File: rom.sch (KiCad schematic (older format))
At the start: 13 parts, among them U3 23128_BASIC, U4 23128_KERNAL, U90 74HCT08

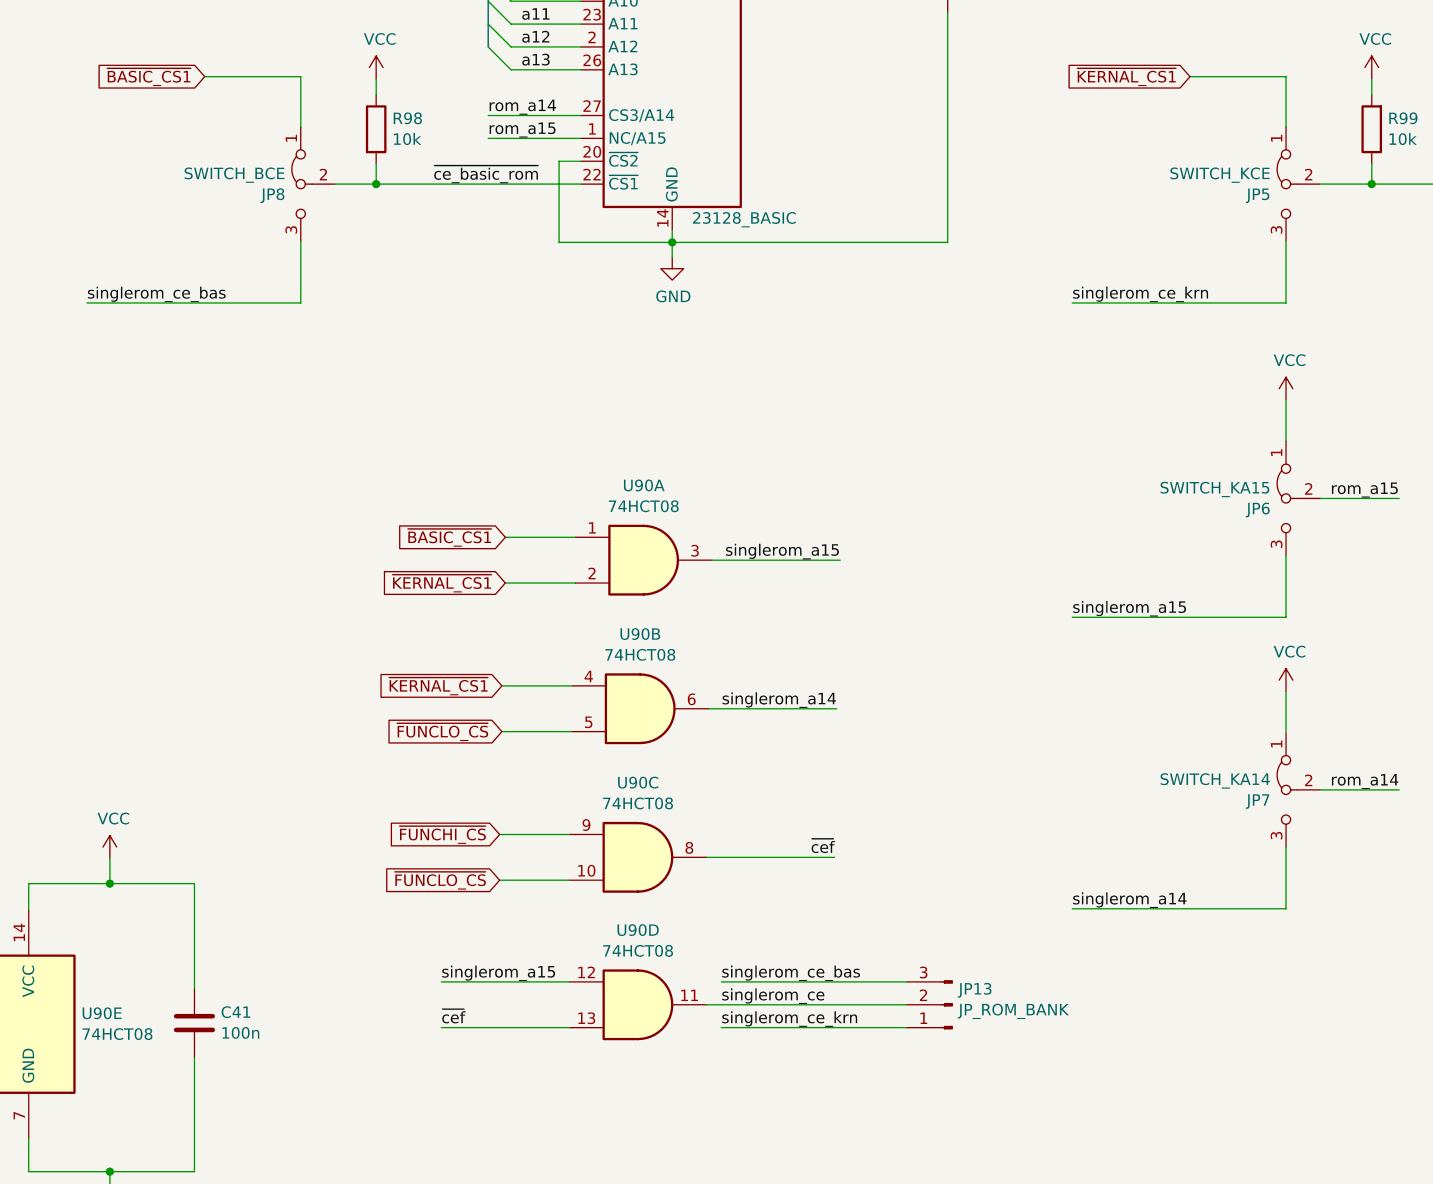
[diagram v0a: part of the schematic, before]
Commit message: Rationalize BOM There should be no significant changes on both schematics on PCB, just some values and something on the silkscreen
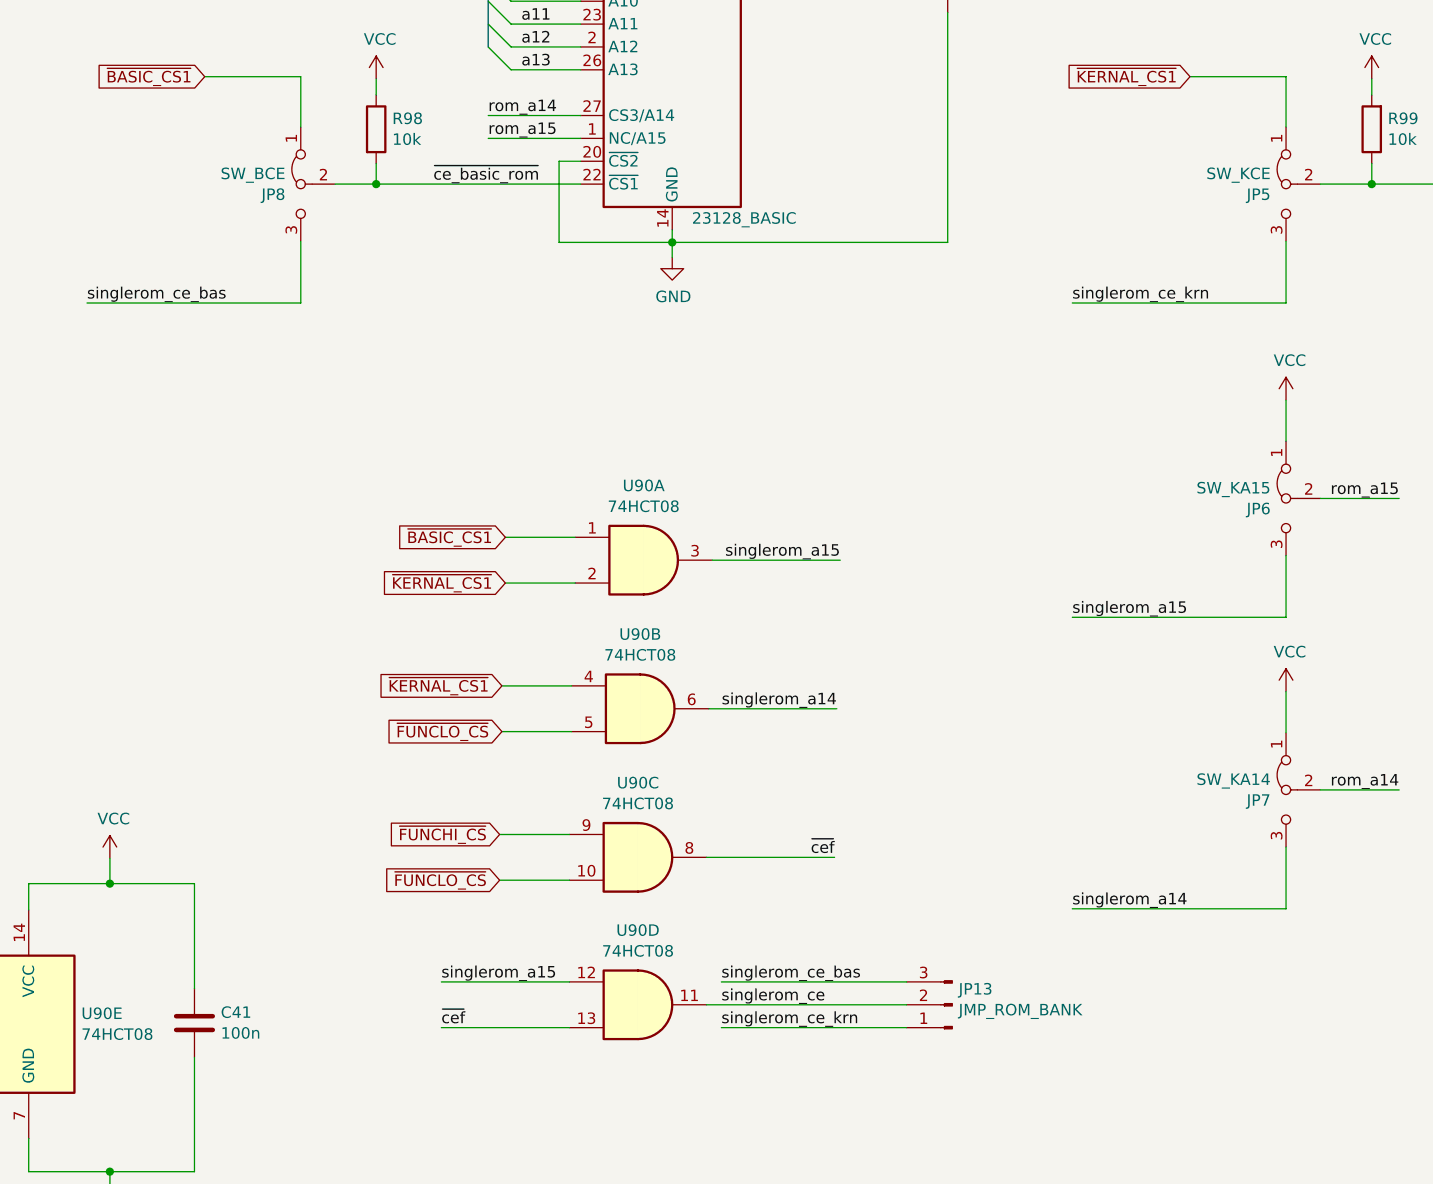
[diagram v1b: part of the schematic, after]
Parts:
- C41, C5, C6: MouserPN (none) -> 810-FG28X7R1H104KNT0
- JP13: value JP_ROM_BANK -> JMP_ROM_BANK
- JP5: value SWITCH_KCE -> SW_KCE
- JP6: value SWITCH_KA15 -> SW_KA15
- JP7: value SWITCH_KA14 -> SW_KA14
- JP8: value SWITCH_BCE -> SW_BCE
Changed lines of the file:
@@
 F 2 "Capacitor_THT:C_Disc_D8.0mm_W2.5mm_P5.00mm" H 4923 1960 50  0001 C CNN
 F 3 "~" H 4885 2110 50  0001 C CNN
+F 4 "810-FG28X7R1H104KNT0" H 4885 2110 50  0001 C CNN "MouserPN"
 	1    4885 2110
 	1    0    0    -1
@@
 F 2 "Capacitor_THT:C_Disc_D8.0mm_W2.5mm_P5.00mm" H 1628 6530 50  0001 C CNN
 F 3 "~" H 1590 6680 50  0001 C CNN
+F 4 "810-FG28X7R1H104KNT0" H 1590 6680 50  0001 C CNN "MouserPN"
 	1    1590 6680
 	1    0    0    -1
@@
 P 6365 3010
 F 0 "JP5" V 6411 3077 50  0000 L CNN
-F 1 "SWITCH_KCE" V 6320 3077 50  0000 L CNN
+F 1 "SW_KCE" V 6320 3077 50  0000 L CNN
 F 2 "Jumper:SolderJumper-3_P1.3mm_Open_RoundedPad1.0x1.5mm" H 6365 3010 50  0001 C CNN
 F 3 "~" H 6365 3010 50  0001 C CNN
@@
 P 6365 5660
 F 0 "JP7" V 6411 5727 50  0000 L CNN
-F 1 "SWITCH_KA14" V 6320 5727 50  0000 L CNN
+F 1 "SW_KA14" V 6320 5727 50  0000 L CNN
 F 2 "Jumper:SolderJumper-3_P1.3mm_Open_RoundedPad1.0x1.5mm" H 6365 5660 50  0001 C CNN
 F 3 "~" H 6365 5660 50  0001 C CNN
@@
 P 6365 4385
 F 0 "JP6" V 6411 4452 50  0000 L CNN
-F 1 "SWITCH_KA15" V 6320 4452 50  0000 L CNN
+F 1 "SW_KA15" V 6320 4452 50  0000 L CNN
 F 2 "Jumper:SolderJumper-3_P1.3mm_Open_RoundedPad1.0x1.5mm" H 6365 4385 50  0001 C CNN
 F 3 "~" H 6365 4385 50  0001 C CNN
@@
 P 2055 3010
 F 0 "JP8" V 2101 3077 50  0000 L CNN
-F 1 "SWITCH_BCE" V 2010 3077 50  0000 L CNN
+F 1 "SW_BCE" V 2010 3077 50  0000 L CNN
 F 2 "Jumper:SolderJumper-3_P1.3mm_Open_RoundedPad1.0x1.5mm" H 2055 3010 50  0001 C CNN
 F 3 "~" H 2055 3010 50  0001 C CNN
@@
 P 4905 6600
 F 0 "JP13" H 4877 6532 50  0000 R CNN
-F 1 "JP_ROM_BANK" H 4877 6623 50  0000 R CNN
+F 1 "JMP_ROM_BANK" H 4877 6623 50  0000 R CNN
 F 2 "Connector_PinHeader_2.54mm:PinHeader_1x03_P2.54mm_Vertical" H 4905 6600 50  0001 C CNN
 F 3 "~" H 4905 6600 50  0001 C CNN
@@
 F 2 "Capacitor_THT:C_Disc_D8.0mm_W2.5mm_P5.00mm" H 9203 1960 50  0001 C CNN
 F 3 "~" H 9165 2110 50  0001 C CNN
+F 4 "810-FG28X7R1H104KNT0" H 9165 2110 50  0001 C CNN "MouserPN"
 	1    9165 2110
 	1    0    0    -1

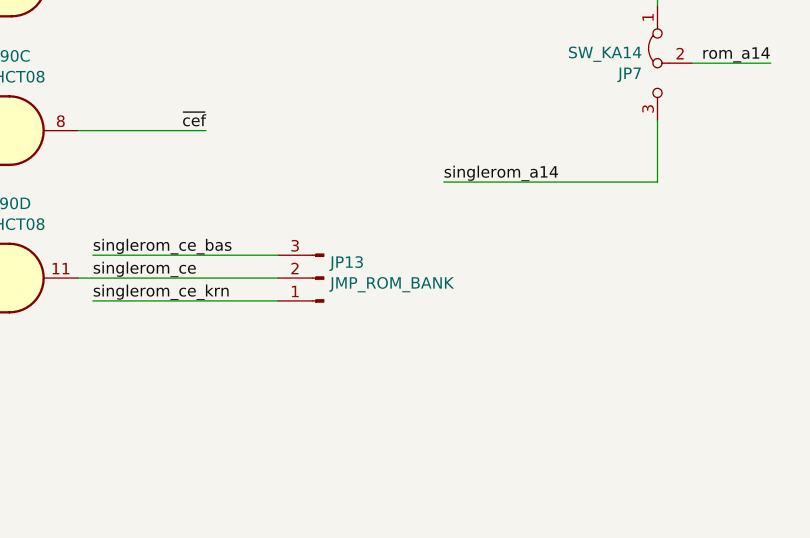
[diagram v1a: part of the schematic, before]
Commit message: Rationalize capacitor footprints & BOM
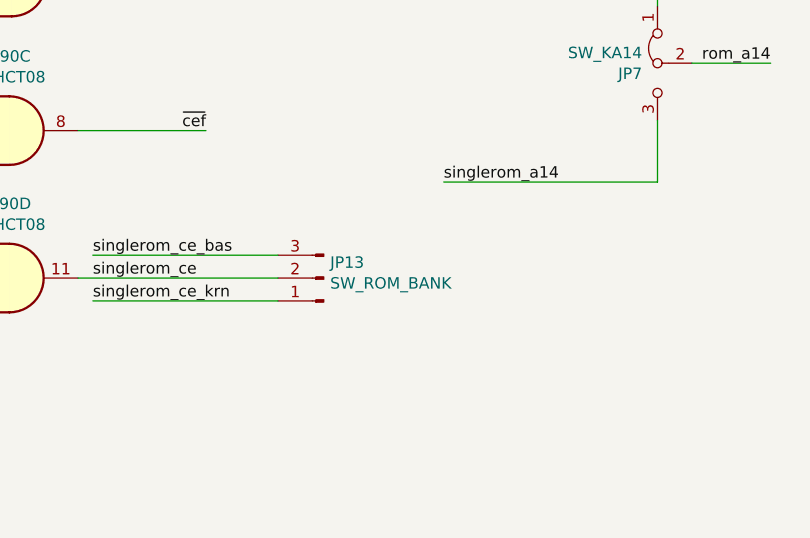
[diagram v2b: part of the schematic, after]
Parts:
- JP13: value JMP_ROM_BANK -> SW_ROM_BANK
- JP5, JP6, JP7, JP8: MouserPN (none) -> ---
- R98, R99: MouserPN (none) -> 603-MFR-25FTF52-10K
- U3, U4: MouserPN (none) -> :); Notes (none) -> Can be replaced with 27512 (E)EPROM
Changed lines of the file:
@@
 F 2 "LittleSixteen:DIP-28_W15.24mm_Socket_LongPads" H 3680 2110 50  0001 C CNN
 F 3 "http://ww1.microchip.com/downloads/en/devicedoc/11003L.pdf" H 3680 2110 50  0001 C CNN
+F 4 ":)" H 3680 2110 50  0001 C CNN "MouserPN"
+F 5 "Can be replaced with 27512 (E)EPROM" H 3680 2110 50  0001 C CNN "Notes"
 	1    3680 2110
 	1    0    0    -1
@@
 F 2 "Jumper:SolderJumper-3_P1.3mm_Open_RoundedPad1.0x1.5mm" H 6365 3010 50  0001 C CNN
 F 3 "~" H 6365 3010 50  0001 C CNN
+F 4 "---" H 6365 3010 50  0001 C CNN "MouserPN"
 	1    6365 3010
 	0    -1   1    0
@@
 F 2 "Jumper:SolderJumper-3_P1.3mm_Open_RoundedPad1.0x1.5mm" H 6365 5660 50  0001 C CNN
 F 3 "~" H 6365 5660 50  0001 C CNN
+F 4 "---" H 6365 5660 50  0001 C CNN "MouserPN"
 	1    6365 5660
 	0    -1   1    0
@@
 F 2 "Jumper:SolderJumper-3_P1.3mm_Open_RoundedPad1.0x1.5mm" H 6365 4385 50  0001 C CNN
 F 3 "~" H 6365 4385 50  0001 C CNN
+F 4 "---" H 6365 4385 50  0001 C CNN "MouserPN"
 	1    6365 4385
 	0    -1   1    0
@@
 F 2 "Jumper:SolderJumper-3_P1.3mm_Open_RoundedPad1.0x1.5mm" H 2055 3010 50  0001 C CNN
 F 3 "~" H 2055 3010 50  0001 C CNN
+F 4 "---" H 2055 3010 50  0001 C CNN "MouserPN"
 	1    2055 3010
 	0    -1   1    0
@@
 P 4905 6600
 F 0 "JP13" H 4877 6532 50  0000 R CNN
-F 1 "JMP_ROM_BANK" H 4877 6623 50  0000 R CNN
+F 1 "SW_ROM_BANK" H 4877 6623 50  0000 R CNN
 F 2 "Connector_PinHeader_2.54mm:PinHeader_1x03_P2.54mm_Vertical" H 4905 6600 50  0001 C CNN
 F 3 "~" H 4905 6600 50  0001 C CNN
@@
 F 2 "Resistor_THT:R_Axial_DIN0207_L6.3mm_D2.5mm_P5.08mm_Vertical" V 2315 2770 50  0001 C CNN
 F 3 "~" H 2385 2770 50  0001 C CNN
+F 4 "603-MFR-25FTF52-10K" H 2385 2770 50  0001 C CNN "MouserPN"
 	1    2385 2770
 	1    0    0    -1
@@
 F 2 "Resistor_THT:R_Axial_DIN0207_L6.3mm_D2.5mm_P5.08mm_Vertical" V 6670 2770 50  0001 C CNN
 F 3 "~" H 6740 2770 50  0001 C CNN
+F 4 "603-MFR-25FTF52-10K" H 6740 2770 50  0001 C CNN "MouserPN"
 	1    6740 2770
 	-1   0    0    1
@@
 F 2 "LittleSixteen:DIP-28_W15.24mm_Socket_LongPads" H 7960 2110 50  0001 C CNN
 F 3 "http://ww1.microchip.com/downloads/en/devicedoc/11003L.pdf" H 7960 2110 50  0001 C CNN
+F 4 ":)" H 7960 2110 50  0001 C CNN "MouserPN"
+F 5 "Can be replaced with 27512 (E)EPROM" H 7960 2110 50  0001 C CNN "Notes"
 	1    7960 2110
 	1    0    0    -1

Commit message: Fix some P/Ns
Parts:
- U90: MouserPN (none) -> 595-SN74HCT08N
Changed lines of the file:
@@
 F 2 "LittleSixteen:DIP-14_W7.62mm_Socket_LongPads" H 3555 4655 50  0001 C CNN
 F 3 "http://www.ti.com/lit/gpn/sn74LS08" H 3555 4655 50  0001 C CNN
+F 4 "595-SN74HCT08N" H 3555 4655 50  0001 C CNN "MouserPN"
 	1    3555 4655
 	1    0    0    -1
@@
 F 2 "LittleSixteen:DIP-14_W7.62mm_Socket_LongPads" H 3540 5305 50  0001 C CNN
 F 3 "http://www.ti.com/lit/gpn/sn74LS08" H 3540 5305 50  0001 C CNN
+F 4 "595-SN74HCT08N" H 3540 5305 50  0001 C CNN "MouserPN"
 	2    3540 5305
 	1    0    0    -1
@@
 F 2 "LittleSixteen:DIP-14_W7.62mm_Socket_LongPads" H 3530 5955 50  0001 C CNN
 F 3 "http://www.ti.com/lit/gpn/sn74LS08" H 3530 5955 50  0001 C CNN
+F 4 "595-SN74HCT08N" H 3530 5955 50  0001 C CNN "MouserPN"
 	3    3530 5955
 	1    0    0    -1
@@
 F 2 "LittleSixteen:DIP-14_W7.62mm_Socket_LongPads" H 3530 6600 50  0001 C CNN
 F 3 "http://www.ti.com/lit/gpn/sn74LS08" H 3530 6600 50  0001 C CNN
+F 4 "595-SN74HCT08N" H 3530 6600 50  0001 C CNN "MouserPN"
 	4    3530 6600
 	1    0    0    -1
@@
 F 2 "LittleSixteen:DIP-14_W7.62mm_Socket_LongPads" H 865 6685 50  0001 C CNN
 F 3 "http://www.ti.com/lit/gpn/sn74LS08" H 865 6685 50  0001 C CNN
+F 4 "595-SN74HCT08N" H 865 6685 50  0001 C CNN "MouserPN"
 	5    865  6685
 	1    0    0    -1
